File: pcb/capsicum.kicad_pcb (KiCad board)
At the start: 2 copper layers, 68.6 x 88.9 mm, 70 parts, among them J2 Screw terminal, J3 USB-C 16+8 USB 2.0, Q1 NS2101P, Q2 BC817, SW1 SW_SPDT, SW3 SW_SPDT, U1 ESP32-C3-WROOM-02, U2 TQ33E-1, U3 AP2112K, U4 MCP73831

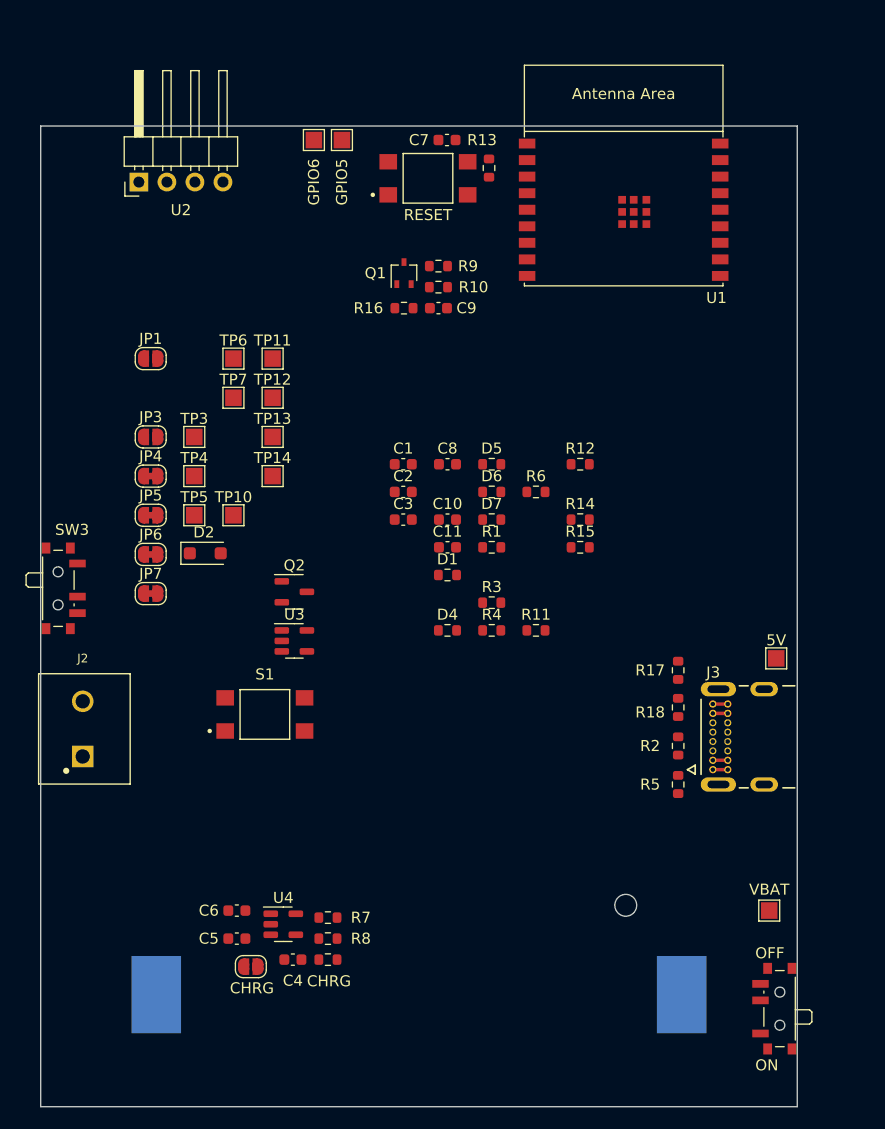
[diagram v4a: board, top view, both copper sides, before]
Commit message: feat: group components from LDO logical block in layout
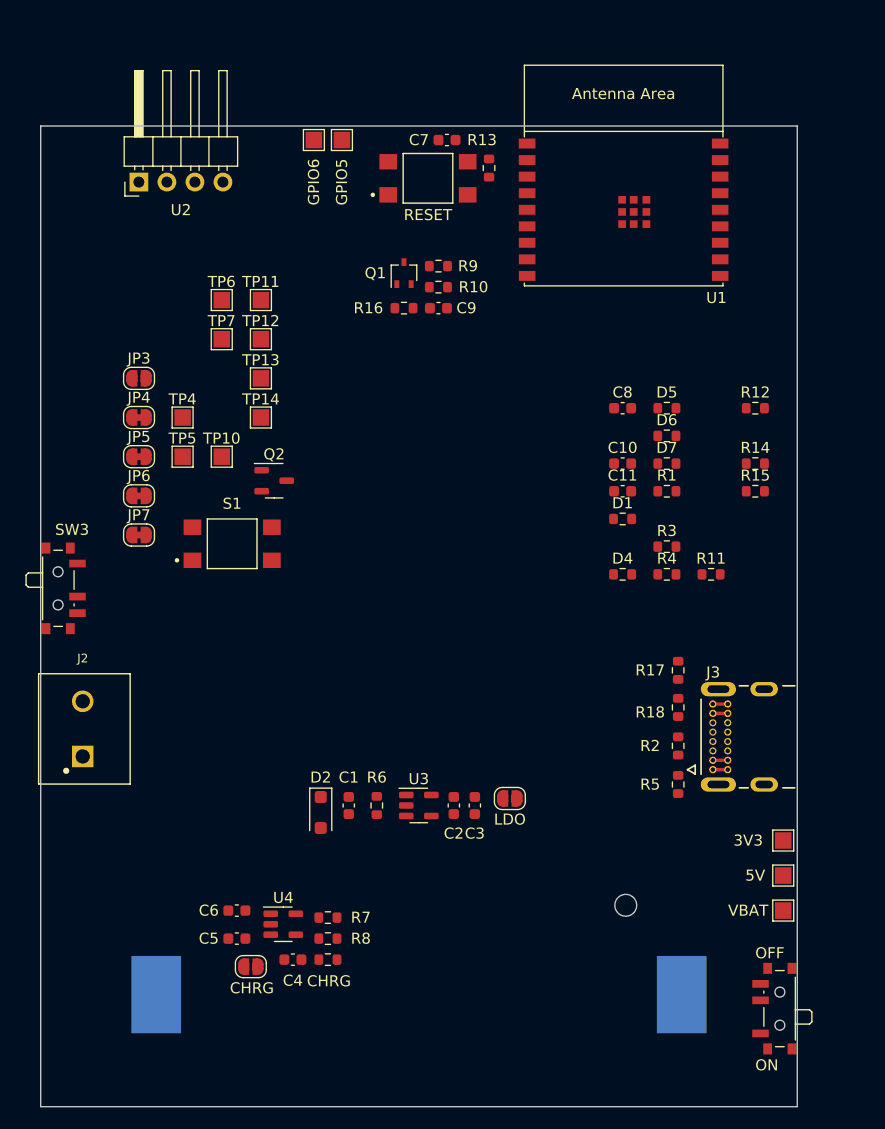
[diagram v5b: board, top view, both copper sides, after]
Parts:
- moved TP3 64.7 mm to (171.4, 115.6)
- moved JP1 51.5 mm to (146.7, 111.8)
- moved R6 31.9 mm to (134.6, 112.4), turned to -90 degrees
- moved C1 31.3 mm to (132.1, 112.4), turned to -90 degrees
- moved C2 28.8 mm to (141.6, 112.4), turned to -90 degrees
- moved C3 26.7 mm to (143.5, 112.4), turned to -90 degrees
- moved D2 25.7 mm to (129.5, 113.0), turned to -90 degrees
- moved 5V 19.7 mm to (171.4, 118.7)
- moved U3 18.7 mm to (138.4, 112.4)
- moved C10 16.7 mm to (156.9, 81.4)
- moved C11 16.7 mm to (156.9, 83.9)
- moved C8 16.7 mm to (156.9, 76.4)
- moved D1 16.7 mm to (156.9, 86.4)
- moved D4 16.7 mm to (156.9, 91.4)
- moved D5 16.7 mm to (160.9, 76.4)
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
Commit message: feat: group components from power LEDs logical block in layout
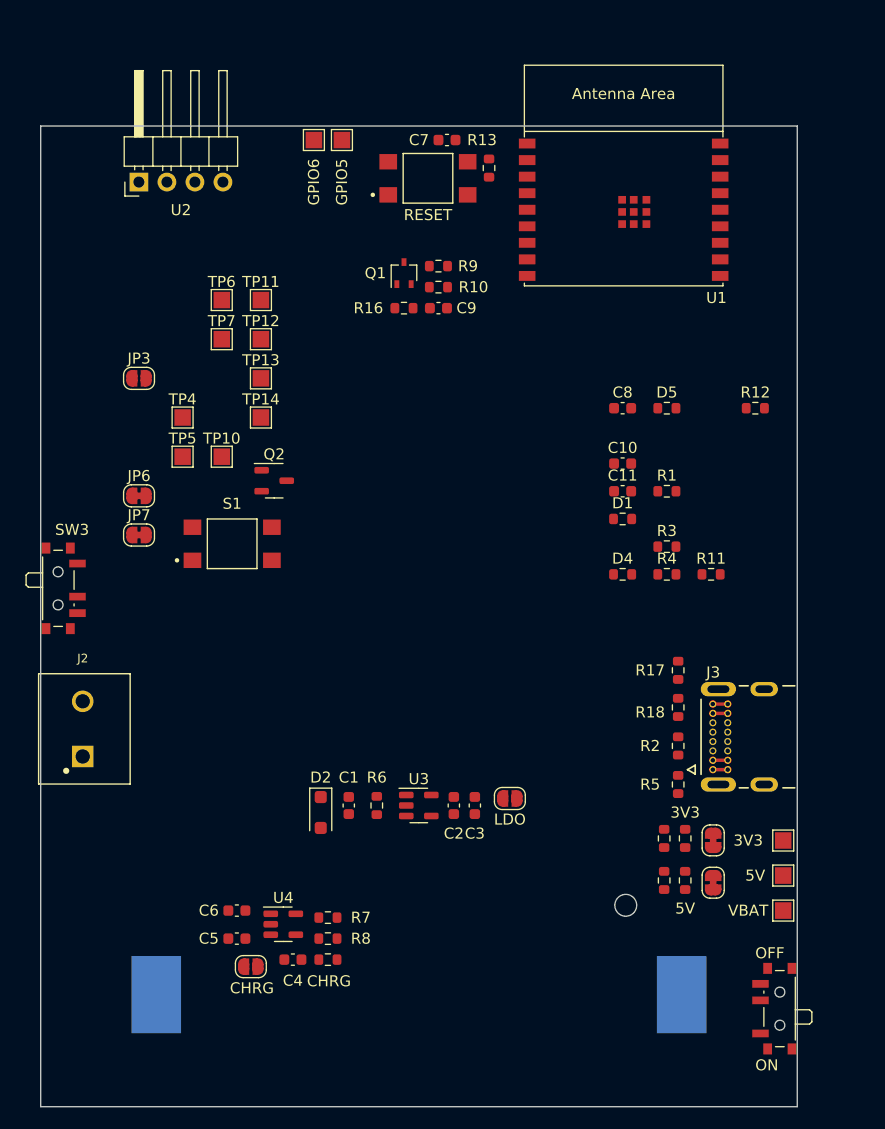
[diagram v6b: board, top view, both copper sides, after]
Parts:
- moved JP4 67.0 mm to (165.1, 119.4), turned to 90 degrees
- moved JP5 62.6 mm to (165.1, 115.6), turned to -90 degrees
- moved D6 40.3 mm to (162.6, 119.2), turned to -90 degrees
- moved R14 38.7 mm to (160.7, 119.2), turned to -90 degrees
- moved D7 34.0 mm to (162.6, 115.4), turned to 90 degrees
- moved R15 32.5 mm to (160.7, 115.4), turned to 90 degrees

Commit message: feat: group components from TX/RX/Status LEDs logical block in layout
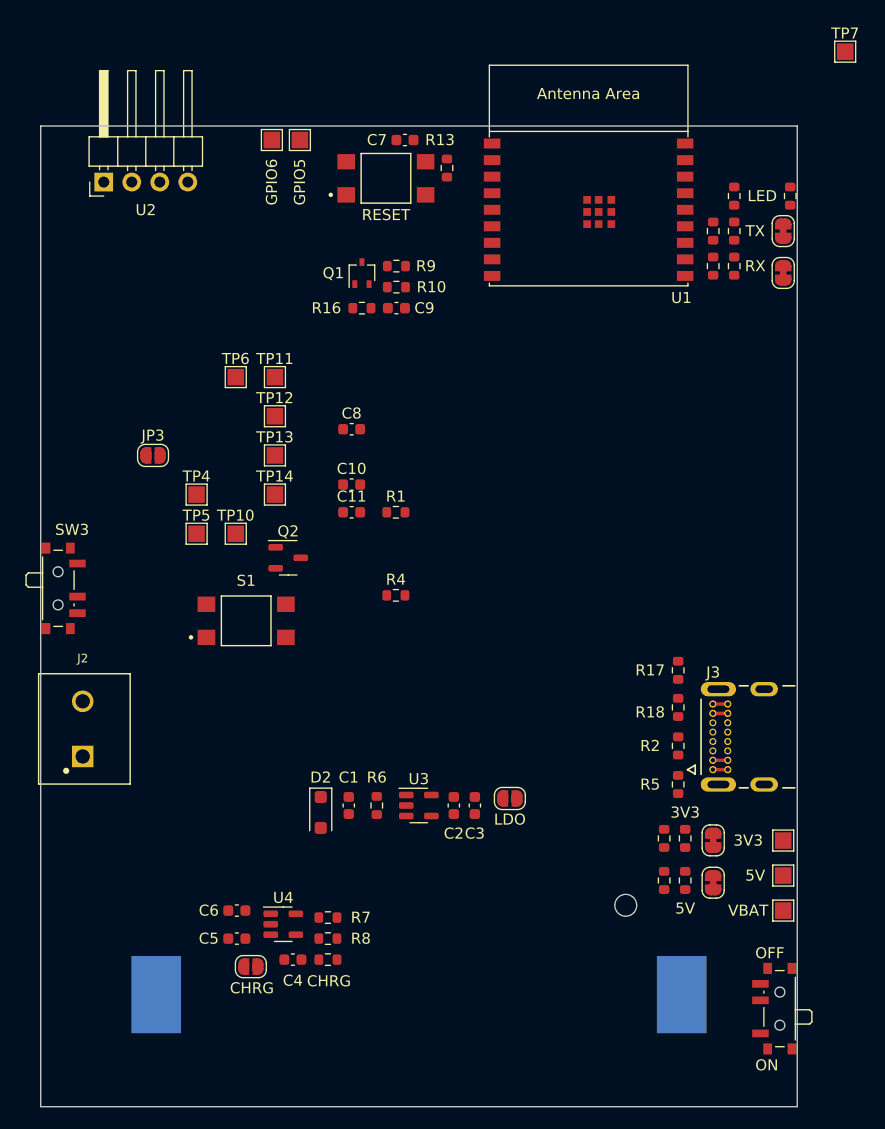
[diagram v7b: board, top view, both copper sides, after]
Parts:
- moved JP6 63.1 mm to (171.4, 60.3), turned to 90 degrees
- moved JP7 63.0 mm to (171.4, 64.1), turned to -90 degrees
- moved TP7 62.2 mm to (177.1, 44.1)
- moved R3 33.7 mm to (172.1, 57.1), turned to 90 degrees
- moved D4 32.7 mm to (167.0, 60.3), turned to -90 degrees
- moved R11 31.1 mm to (165.1, 60.3), turned to -90 degrees
- moved D1 31.0 mm to (167.0, 57.1), turned to 90 degrees
- moved C10 24.6 mm to (132.3, 83.3)
- moved C11 24.6 mm to (132.3, 85.8)
- moved C8 24.6 mm to (132.3, 78.3)
- moved R1 24.6 mm to (136.3, 85.8)
- moved R4 24.6 mm to (136.3, 93.3)
- moved D5 14.3 mm to (167.0, 63.5), turned to 90 degrees
- moved R12 13.4 mm to (165.1, 63.5), turned to 90 degrees
- moved JP3 7.10 mm to (114.3, 80.7)
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
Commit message: feat: group components from sleep-check logical block in layout
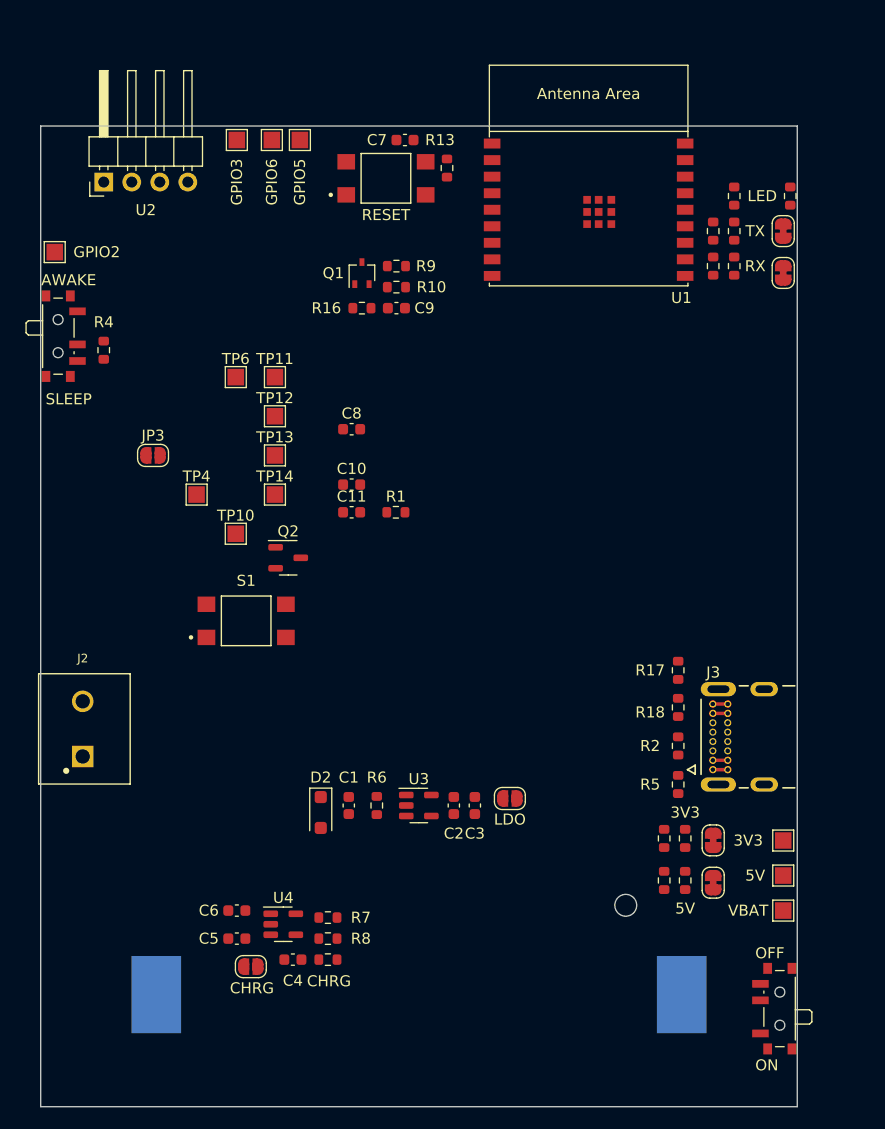
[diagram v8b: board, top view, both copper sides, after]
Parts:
- moved TP7 55.7 mm to (121.9, 52.1)
- moved R4 34.6 mm to (109.9, 71.1), turned to 90 degrees
- moved TP5 28.6 mm to (105.4, 62.2)
- moved SW3 22.9 mm to (106.0, 69.8)
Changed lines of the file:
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@@
   )
   (footprint "TestPoint:TestPoint_Pad_1.5x1.5mm" (layer "F.Cu")
-    (at 118.2725 87.76)
+    (at 105.41 62.23)
     (descr "SMD rectangular pad as test Point, square 1.5mm side length")
     (tags "test point SMD pad rectangle square")
@@
     (property "ki_keywords" "test point tp")
     (attr exclude_from_pos_files)
-    (fp_text reference "TP5" (at 0 -1.648) (layer "F.SilkS")
+    (fp_text reference "TP5" (at 0 -1.648) (layer "F.SilkS") hide
         (effects (font (size 1 1) (thickness 0.15)))
     )
@@
         (effects (font (size 1 1) (thickness 0.15)))
     )
+    (fp_text user "GPIO2" (at 3.81 0 unlocked) (layer "F.SilkS")
+        (effects (font (size 1 1) (thickness 0.15)))
+    )
     (fp_text user "${REFERENCE}" (at 0 -1.65) (layer "F.Fab")
         (effects (font (size 1 1) (thickness 0.15)))
@@
   )
   (footprint "Button_Switch_SMD:SW_SPDT_PCM12" (layer "F.Cu")
-    (at 106.045 92.71 -90)
+    (at 106.045 69.85 -90)
     (descr "Ultraminiature Surface Mount Slide Switch, right-angle, https://www.ckswitches.com/media/1424/pcm.pdf")
     (property "Category" "Electronics")
@@
     (property "ki_keywords" "switch single-pole double-throw spdt ON-ON")
     (attr smd)
-    (fp_text reference "SW3" (at -5.31 -0.94) (layer "F.SilkS")
+    (fp_text reference "SW3" (at -5.31 -0.94) (layer "F.SilkS") hide
         (effects (font (size 1 1) (thickness 0.15)))
     )
@@
         (effects (font (size 1 1) (thickness 0.15)))
     )
+    (fp_text user "AWAKE" (at -5.08 -0.635 unlocked) (layer "F.SilkS")
+        (effects (font (size 1 1) (thickness 0.15)))
+    )
+    (fp_text user "SLEEP" (at 5.715 -0.635 unlocked) (layer "F.SilkS")
+        (effects (font (size 1 1) (thickness 0.15)))
+    )
     (fp_text user "${REFERENCE}" (at -5.31 -0.94) (layer "F.Fab")
         (effects (font (size 1 1) (thickness 0.15)))
@@
   )
   (footprint "Resistor_SMD:R_0603_1608Metric" (layer "F.Cu")
-    (at 136.335 93.345)
+    (at 109.855 71.12 90)
     (descr "Resistor SMD 0603 (1608 Metric), square (rectangular) end terminal, IPC_7351 nominal, (Body size source: IPC-SM-782 page 72, https://www.pcb-3d.com/wordpress/wp-content/uploads/ipc-sm-782a_amendment_1_and_2.pdf), generated with kicad-footprint-generator")
     (tags "resistor")
@@
     (property "ki_keywords" "R resistor")
     (attr smd)
-    (fp_text reference "R4" (at 0 -1.43) (layer "F.SilkS")
+    (fp_text reference "R4" (at 2.54 0 180) (layer "F.SilkS")
         (effects (font (size 1 1) (thickness 0.15)))
     )
-    (fp_text value "1k" (at 0 1.43) (layer "F.Fab")
+    (fp_text value "1k" (at 0 1.43 90) (layer "F.Fab")
         (effects (font (size 1 1) (thickness 0.15)))
     )
-    (fp_text user "${REFERENCE}" (at 0 0) (layer "F.Fab")
+    (fp_text user "${REFERENCE}" (at 0 0 90) (layer "F.Fab")
         (effects (font (size 0.4 0.4) (thickness 0.06)))
     )
@@
     (fp_line (start 0.8 0.4125) (end -0.8 0.4125)
       (stroke (width 0.1) (type solid)) (layer "F.Fab"))
-    (pad "1" smd roundrect (at -0.825 0) (size 0.8 0.95) (layers "F.Cu" "F.Paste" "F.Mask") (roundrect_rratio 0.25)
+    (pad "1" smd roundrect (at -0.825 0 90) (size 0.8 0.95) (layers "F.Cu" "F.Paste" "F.Mask") (roundrect_rratio 0.25)
       (net 35 "Net-(SW3-C)") (pintype "passive"))
-    (pad "2" smd roundrect (at 0.825 0) (size 0.8 0.95) (layers "F.Cu" "F.Paste" "F.Mask") (roundrect_rratio 0.25)
+    (pad "2" smd roundrect (at 0.825 0 90) (size 0.8 0.95) (layers "F.Cu" "F.Paste" "F.Mask") (roundrect_rratio 0.25)
       (net 2 "GND") (pintype "passive"))
     (model "${KICAD6_3DMODEL_DIR}/Resistor_SMD.3dshapes/R_0603_1608Metric.wrl"
@@
   )
   (footprint "TestPoint:TestPoint_Pad_1.5x1.5mm" (layer "F.Cu")
-    (at 177.0675 44.06)
+    (at 121.92 52.07)
     (descr "SMD rectangular pad as test Point, square 1.5mm side length")
     (tags "test point SMD pad rectangle square")
@@
     (property "ki_keywords" "test point tp")
     (attr exclude_from_pos_files)
-    (fp_text reference "TP7" (at 0 -1.648) (layer "F.SilkS")
+    (fp_text reference "TP7" (at 0 -1.648) (layer "F.SilkS") hide
         (effects (font (size 1 1) (thickness 0.15)))
     )
@@
         (effects (font (size 1 1) (thickness 0.15)))
     )
+    (fp_text user "GPIO3" (at 0 3.81 90 unlocked) (layer "F.SilkS")
+        (effects (font (size 1 1) (thickness 0.15)))
+    )
